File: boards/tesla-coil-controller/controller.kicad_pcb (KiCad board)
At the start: 2 copper layers, 163 x 141.8 mm, 331 parts, among them J1 DF40C-40DP-0.4V(51), J10 AUX 4 / 0-5V, J2 DF40C(2.0)-40DS-0.4V(51), J3 AUX 1 / 0-5V, J30 12V BATTERY / LOWER, J4 12V BATTERY / UPPER, J40 CST SECONDARY, J5 USB-C / PROGRAMMING ONLY, J50 GDT 1 PRIMARY, J51 GDT 2 PRIMARY, J60 CST 2 SECONDARY, J8 AUX 2 / 0-5V, J9 AUX 3 / 0-5V, Q50 STD80N10F7, Q51 STD80N10F7, Q52 STD80N10F7, Q53 STD80N10F7, Q54 STD80N10F7, Q55 STD80N10F7, Q56 STD80N10F7, Q57 STD80N10F7, U1 AD7606C-16BSTZ, U2 AP2112K-3.3, U3 USBLC6-2SC6, U30 LMZ14202HTZX/NOPB, U31 LMZ14202HTZX/NOPB, U40 OPA197IDBVR, U41 OPA197IDBVR, U42 TLV3501AIDBVR, U44 TPS60403DBVR, U51 UCC27282DR, U52 UCC27282DR, U53 UCC27282DR, U54 UCC27282DR, U60 OPA197IDBVR, U61 OPA197IDBVR, U62 TLV3501AIDBVR, U70 OPA197IDBVR, U71 OPA197IDBVR, U72 OPA197IDBVR, U73 OPA197IDBVR

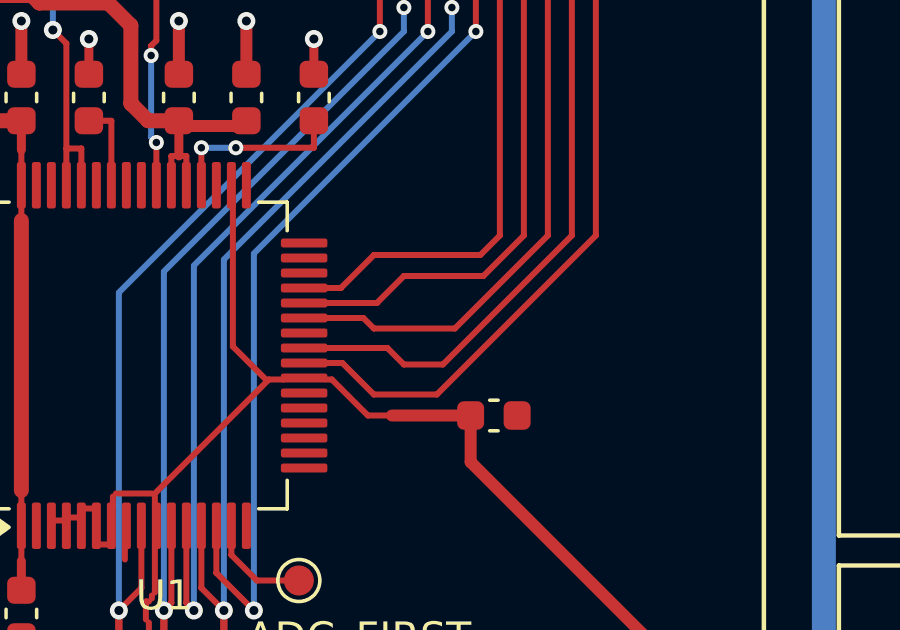
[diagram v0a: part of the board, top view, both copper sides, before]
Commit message: Groom the ADC data-line exits into one horizontal and one 45° climb each
Portal edit-stack item: "The lines to the right of the adc could be nicer
groomed". ADC_SDI and ADC_DOUT_A..D each left the ADC with a horizontal, a
45° jog to a different row (some up, some down, all different sizes), a
second horizontal, and a 45° climb into the 0.8 mm column bus at y=92. The
jogs did the 0.5 -> 0.8 mm pitch change and looked ragged.

Each line is now a single straight horizontal from its pad at its own pin
row, then one 45° climb landing on the same column endpoint as before. The
pitch change happens in the diagonal start points instead of mid-run jogs.
Four segments per net became two; the column verticals are untouched.

Generator-owned: tesla_reviewed_routing.json edited and replayed. No
footprints moved; only the five ADC nets changed. DRC 0/0/0. kct lint:
0 open; five flagged findings on these lines (four route.bend_count and the
ADC_DOUT_D route.redundant_bend) are resolved and their exceptions removed.
Evidence refreshed for the remaining 188 exceptions (132 ignored, 56 flagged).

Co-Authored-By: Claude Fable 5.1 <noreply@anthropic.com>
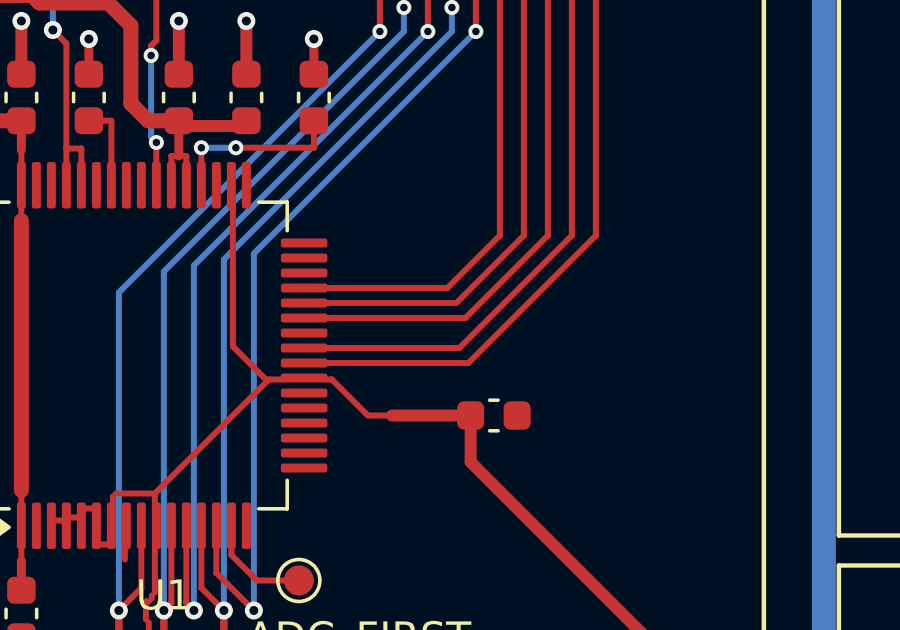
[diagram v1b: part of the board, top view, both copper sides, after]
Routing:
- net ADC_DOUT_A: track 36.2 -> 35.3 mm
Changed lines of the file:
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@@
 	(segment
 		(start 98.675 93.75)
-		(end 99.9 93.75)
-		(width 0.2)
-		(layer "F.Cu")
-		(net "ADC_SDI")
-	)
-	(segment
-		(start 104.55 92.65)
-		(end 101 92.65)
-		(width 0.2)
-		(layer "F.Cu")
-		(net "ADC_SDI")
-	)
-	(segment
-		(start 99.9 93.75)
-		(end 101 92.65)
-		(width 0.2)
-		(layer "F.Cu")
-		(net "ADC_SDI")
-	)
-	(segment
-		(start 105.2 92)
-		(end 104.55 92.65)
+		(end 103.45 93.75)
 		(width 0.2)
 		(layer "F.Cu")
@@
 	(segment
 		(start 105.2 68.82)
+		(end 105.2 92)
+		(width 0.2)
+		(layer "F.Cu")
+		(net "ADC_SDI")
+	)
+	(segment
+		(start 103.45 93.75)
 		(end 105.2 92)
 		(width 0.2)
@@
 	)
 	(segment
-		(start 98.675 94.25)
-		(end 101.1 94.25)
-		(width 0.2)
-		(layer "F.Cu")
-		(net "ADC_DOUT_D")
-	)
-	(segment
 		(start 105.6 71.6)
 		(end 106 72)
@@
 	)
 	(segment
-		(start 106 92)
-		(end 104.65 93.35)
+		(start 98.675 94.25)
+		(end 103.75 94.25)
 		(width 0.2)
 		(layer "F.Cu")
@@
 	)
 	(segment
-		(start 101.1 94.25)
-		(end 102 93.35)
+		(start 103.75 94.25)
+		(end 106 92)
 		(width 0.2)
 		(layer "F.Cu")
@@
 	)
 	(segment
-		(start 104.65 93.35)
-		(end 102 93.35)
-		(width 0.2)
-		(layer "F.Cu")
-		(net "ADC_DOUT_D")
-	)
-	(segment
-		(start 106.8 92)
-		(end 103.7 95.1)
-		(width 0.2)
-		(layer "F.Cu")
-		(net "ADC_DOUT_C")
-	)
-	(segment
-		(start 100.65 94.75)
-		(end 101 95.1)
-		(width 0.2)
-		(layer "F.Cu")
-		(net "ADC_DOUT_C")
-	)
-	(segment
-		(start 98.675 94.75)
-		(end 100.65 94.75)
-		(width 0.2)
-		(layer "F.Cu")
-		(net "ADC_DOUT_C")
-	)
-	(segment
 		(start 106 68.82)
 		(end 106 71.2)
-		(width 0.2)
-		(layer "F.Cu")
-		(net "ADC_DOUT_C")
-	)
-	(segment
-		(start 103.7 95.1)
-		(end 101 95.1)
 		(width 0.2)
 		(layer "F.Cu")
@@
 	)
 	(segment
+		(start 98.675 94.75)
+		(end 104.05 94.75)
+		(width 0.2)
+		(layer "F.Cu")
+		(net "ADC_DOUT_C")
+	)
+	(segment
 		(start 106.8 72)
+		(end 106.8 92)
+		(width 0.2)
+		(layer "F.Cu")
+		(net "ADC_DOUT_C")
+	)
+	(segment
+		(start 104.05 94.75)
 		(end 106.8 92)
 		(width 0.2)
@@
 	)
 	(segment
-		(start 103.3 96.3)
-		(end 102 96.3)
+		(start 98.675 95.75)
+		(end 103.85 95.75)
+		(width 0.2)
+		(layer "F.Cu")
+		(net "ADC_DOUT_B")
+	)
+	(segment
+		(start 103.85 95.75)
+		(end 107.6 92)
 		(width 0.2)
 		(layer "F.Cu")
@@
 	)
 	(segment
-		(start 107.6 92)
-		(end 103.3 96.3)
-		(width 0.2)
-		(layer "F.Cu")
-		(net "ADC_DOUT_B")
-	)
-	(segment
 		(start 106.4 70.8)
 		(end 107.6 72)
-		(width 0.2)
-		(layer "F.Cu")
-		(net "ADC_DOUT_B")
-	)
-	(segment
-		(start 101.45 95.75)
-		(end 102 96.3)
-		(width 0.2)
-		(layer "F.Cu")
-		(net "ADC_DOUT_B")
-	)
-	(segment
-		(start 98.675 95.75)
-		(end 101.45 95.75)
 		(width 0.2)
 		(layer "F.Cu")
@@
 	)
 	(segment
-		(start 108.4 91.999999)
-		(end 103.1 97.3)
-		(width 0.2)
-		(layer "F.Cu")
-		(net "ADC_DOUT_A")
-	)
-	(segment
-		(start 98.675 96.25)
-		(end 99.95 96.25)
-		(width 0.2)
-		(layer "F.Cu")
-		(net "ADC_DOUT_A")
-	)
-	(segment
 		(start 106.8 70.4)
 		(end 108.4 72)
@@
 	)
 	(segment
-		(start 99.95 96.25)
-		(end 101 97.3)
+		(start 104.15 96.25)
+		(end 108.4 92)
 		(width 0.2)
 		(layer "F.Cu")
@@
 	)
 	(segment
-		(start 103.1 97.3)
-		(end 101 97.3)
+		(start 98.675 96.25)
+		(end 104.15 96.25)
 		(width 0.2)
 		(layer "F.Cu")

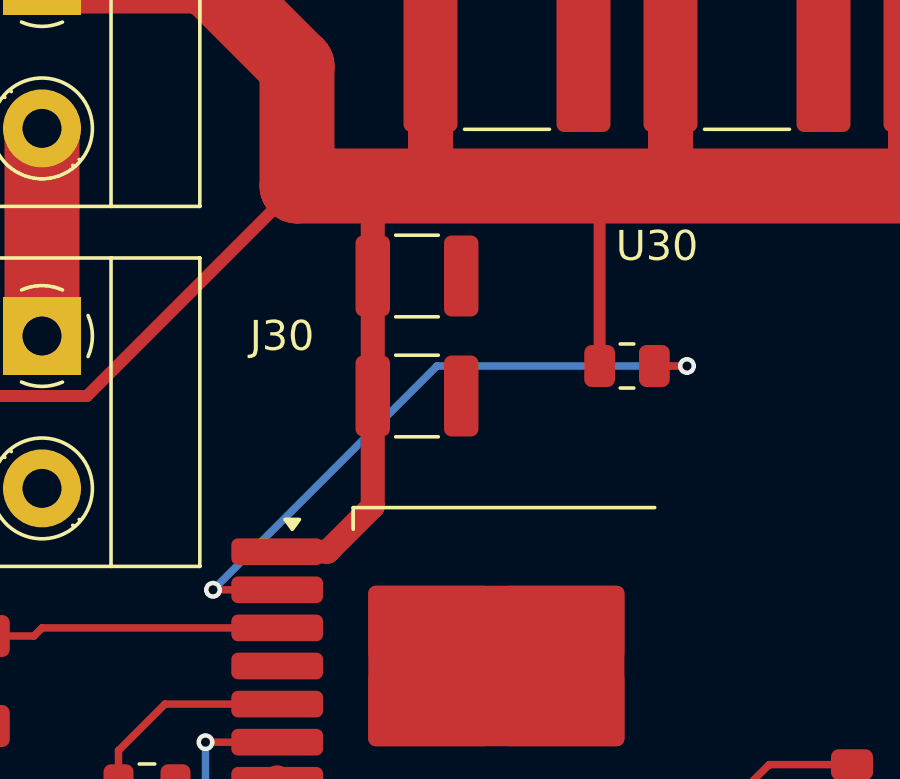
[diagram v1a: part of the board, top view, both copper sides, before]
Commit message: Move R302 next to U30 so P30_RON no longer runs under C302
Portal edit-stack item: "Move this guy so under-trace is unneeded". R302
(249k RON resistor) sat at (47,52) on the far side of the input caps, so
P30_RON dropped to B.Cu at its pad, ran 8 mm under C302, and came back up
beside U30 pin 2. R302 now sits at (35.1,55.55), rotated 180, in the gap
between J30's courtyard and the top of U30. RON leaves pad 2 straight,
wraps around U30 pin 1 at x=33.3 and enters pin 2 straight; VBAT leaves
pad 1 straight and tees into the 0.8 mm VBAT bus at full width. Both vias
and both B.Cu segments are gone, as is the old VBAT stub that fed R302
from the y=46 bus.

Also fixes the UUID suffixes of the ADC exit segments added in 5742a12
(non-hex characters made KiCad regenerate them on every replay).

Generator-owned: tesla_placement.json and tesla_reviewed_routing.json
edited and replayed. Only R302 moved; only P30_RON and VBAT_24V copper
changed. DRC 0/0/0 (kicad-cli and kicadmium). kct lint: 0 open, no new
findings; evidence refreshed for all 188 exceptions (132 ignored, 56 flagged).

Co-Authored-By: Claude Fable 5.1 <noreply@anthropic.com>
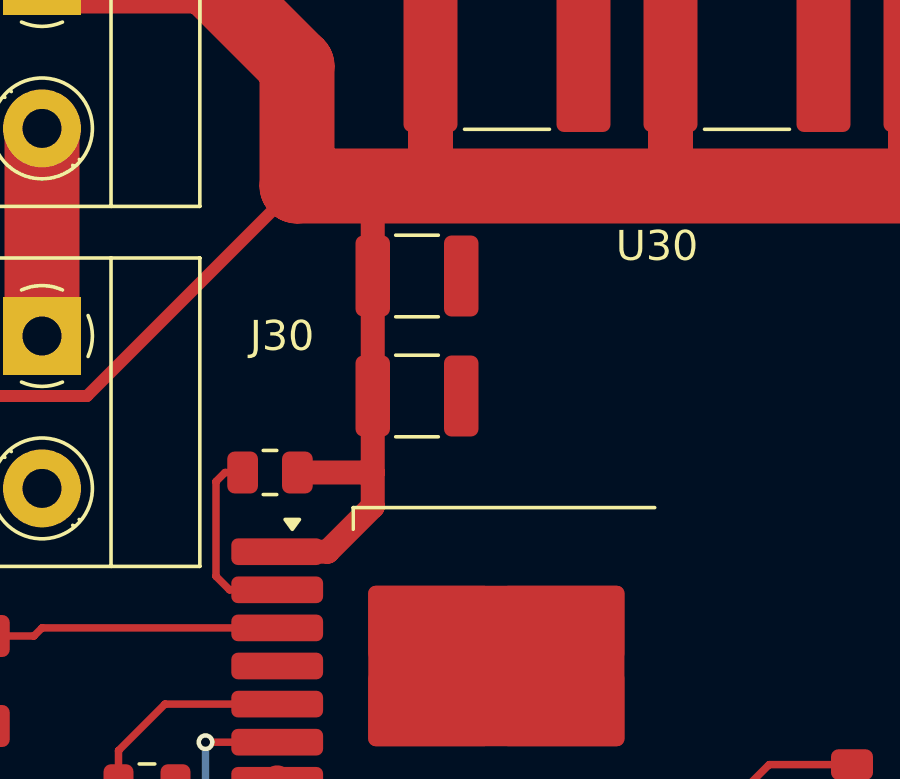
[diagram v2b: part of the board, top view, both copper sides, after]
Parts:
- moved R302 12.4 mm to (35.1, 55.5), turned to 180 degrees
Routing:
- net P30_RON: track 22.1 -> 6.40 mm, vias 2 -> 0
- net VBAT_24V: track 607.8 -> 604.3 mm
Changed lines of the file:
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@@
 	(footprint "Tesla:R_0805_2012Metric"
 		(layer "F.Cu")
-		(at 47 52)
+		(at 35.1 55.55 180)
 		(descr "Resistor SMD 0805 (2012 Metric), square (rectangular) end terminal, IPC_7351 nominal, (Body size source: IPC-SM-782 page 72, https://www.pcb-3d.com/wordpress/wp-content/uploads/ipc-sm-782a_amendment_1_and_2.pdf), generated with kicad-footprint-generator")
 		(tags "resistor")
 		(property "Reference" "R302"
-			(at 0 -5 0)
+			(at 0 1.1 180)
 			(layer "F.SilkS")
 			(hide yes)
@@
 		)
 		(property "Value" "249k"
-			(at 0 1.65 0)
+			(at 0 1.65 180)
 			(layer "F.Fab")
 			(hide yes)
@@
 		)
 		(property "Datasheet" ""
-			(at 0 0 0)
+			(at 0 0 180)
 			(layer "F.Fab")
 			(hide yes)
@@
 		)
 		(property "Description" ""
-			(at 0 0 0)
+			(at 0 0 180)
 			(layer "F.Fab")
 			(hide yes)
@@
 		)
 		(property "MPN" ""
-			(at 0 0 0)
+			(at 0 0 180)
 			(layer "F.SilkS")
 			(hide yes)
@@
 		)
 		(property "LCSC" ""
-			(at 0 0 0)
+			(at 0 0 180)
 			(layer "F.SilkS")
 			(hide yes)
@@
 		)
 		(property "Design status" "Acquisition draft / not for fabrication"
-			(at 0 0 0)
+			(at 0 0 180)
 			(layer "F.SilkS")
 			(hide yes)
@@
 		(duplicate_pad_numbers_are_jumpers no)
 		(fp_line
-			(start -0.227064 -0.735)
-			(end 0.227064 -0.735)
+			(start -0.227064 0.735)
+			(end 0.227064 0.735)
 			(stroke
 				(width 0.12)
@@
 		)
 		(fp_line
-			(start -0.227064 0.735)
-			(end 0.227064 0.735)
+			(start -0.227064 -0.735)
+			(end 0.227064 -0.735)
 			(stroke
 				(width 0.12)
@@
 		)
 		(fp_line
-			(start -1.68 -0.95)
-			(end 1.68 -0.95)
+			(start 1.68 0.95)
+			(end -1.68 0.95)
 			(stroke
 				(width 0.05)
@@
 		)
 		(fp_line
-			(start -1.68 0.95)
-			(end -1.68 -0.95)
+			(start 1.68 -0.95)
+			(end 1.68 0.95)
 			(stroke
 				(width 0.05)
@@
 		)
 		(fp_line
-			(start 1.68 -0.95)
-			(end 1.68 0.95)
+			(start -1.68 0.95)
+			(end -1.68 -0.95)
 			(stroke
 				(width 0.05)
@@
 		)
 		(fp_line
-			(start 1.68 0.95)
-			(end -1.68 0.95)
+			(start -1.68 -0.95)
+			(end 1.68 -0.95)
 			(stroke
 				(width 0.05)
@@
 		)
 		(fp_line
-			(start -1 -0.625)
-			(end 1 -0.625)
+			(start 1 0.625)
+			(end -1 0.625)
 			(stroke
 				(width 0.1)
@@
 		)
 		(fp_line
-			(start -1 0.625)
-			(end -1 -0.625)
+			(start 1 -0.625)
+			(end 1 0.625)
 			(stroke
 				(width 0.1)
@@
 		)
 		(fp_line
-			(start 1 -0.625)
-			(end 1 0.625)
+			(start -1 0.625)
+			(end -1 -0.625)
 			(stroke
 				(width 0.1)
@@
 		)
 		(fp_line
-			(start 1 0.625)
-			(end -1 0.625)
+			(start -1 -0.625)
+			(end 1 -0.625)
 			(stroke
 				(width 0.1)
@@
 		)
 		(fp_text user "${REFERENCE}"
-			(at 0 0 0)
+			(at 0 0 180)
 			(layer "F.Fab")
 			(effects
@@
 		)
 		(pad "1" smd roundrect
-			(at -0.9125 0)
+			(at -0.9125 0 180)
 			(size 1.025 1.4)
 			(layers "F.Cu" "F.Mask" "F.Paste")
@@
 		)
 		(pad "2" smd roundrect
-			(at 0.9125 0)
+			(at 0.9125 0 180)
 			(size 1.025 1.4)
 			(layers "F.Cu" "F.Mask" "F.Paste")
@@
 	)
 	(segment
+		(start 36.0125 55.55)
+		(end 38.525 55.55)
+		(width 0.8)
+		(layer "F.Cu")
+		(net "VBAT_24V")
+	)
+	(segment
 		(start 71.525 56.685)
 		(end 70.02 58.19)
@@
 	)
 	(segment
-		(start 46.0875 46)
-		(end 46.0875 52)
-		(width 0.4)
-		(layer "F.Cu")
-		(net "VBAT_24V")
-	)
-	(segment
 		(start 35 39)
 		(end 34 40)
@@
 	)
 	(segment
-		(start 105.2 68.82)
+		(start 103.45 93.75)
 		(end 105.2 92)
 		(width 0.2)
@@
 	)
 	(segment
-		(start 103.45 93.75)
+		(start 105.2 68.82)
 		(end 105.2 92)
 		(width 0.2)
@@
 	)
 	(segment
-		(start 105.6 71.6)
-		(end 106 72)
+		(start 98.675 94.25)
+		(end 103.75 94.25)
 		(width 0.2)
 		(layer "F.Cu")
@@
 	)
 	(segment
-		(start 98.675 94.25)
-		(end 103.75 94.25)
+		(start 103.75 94.25)
+		(end 106 92)
 		(width 0.2)
 		(layer "F.Cu")
@@
 	)
 	(segment
-		(start 103.75 94.25)
-		(end 106 92)
+		(start 105.6 71.6)
+		(end 106 72)
 		(width 0.2)
 		(layer "F.Cu")
@@
 	)
 	(segment
-		(start 106 68.82)
-		(end 106 71.2)
+		(start 98.675 94.75)
+		(end 104.05 94.75)
 		(width 0.2)
 		(layer "F.Cu")
@@
 	)
 	(segment
-		(start 106 71.2)
-		(end 106.8 72)
+		(start 104.05 94.75)
+		(end 106.8 92)
 		(width 0.2)
 		(layer "F.Cu")
@@
 	)
 	(segment
-		(start 98.675 94.75)
-		(end 104.05 94.75)
+		(start 106 68.82)
+		(end 106 71.2)
 		(width 0.2)
 		(layer "F.Cu")
@@
 	)
 	(segment
-		(start 106.8 72)
-		(end 106.8 92)
+		(start 106 71.2)
+		(end 106.8 72)
 		(width 0.2)
 		(layer "F.Cu")
@@
 	)
 	(segment
-		(start 104.05 94.75)
+		(start 106.8 72)
 		(end 106.8 92)
 		(width 0.2)
@@
 	)
 	(segment
-		(start 106.8 70.4)
-		(end 108.4 72)
+		(start 98.675 96.25)
+		(end 104.15 96.25)
 		(width 0.2)
 		(layer "F.Cu")
@@
 	)
 	(segment
-		(start 98.675 96.25)
-		(end 104.15 96.25)
+		(start 106.8 70.4)
+		(end 108.4 72)
 		(width 0.2)
 		(layer "F.Cu")
@@
 	)
 	(segment
-		(start 47.9125 52)
-		(end 49 52)
+		(start 34.1875 55.55)
+		(end 33.6 55.55)
 		(width 0.25)
 		(layer "F.Cu")
@@
 	)
 	(segment
-		(start 35.34 59.46)
-		(end 33.2 59.46)
+		(start 33.6 55.55)
+		(end 33.3 55.85)
 		(width 0.25)
 		(layer "F.Cu")
 		(net "P30_RON")
 	)
-	(via
-		(at 33.2 59.46)
-		(size 0.6)
-		(drill 0.3)
-		(layers "F.Cu" "B.Cu")
-		(net "P30_RON")
-	)
-	(via
-		(at 49 52)
-		(size 0.6)
-		(drill 0.3)
-		(layers "F.Cu" "B.Cu")
+	(segment
+		(start 33.3 55.85)
+		(end 33.3 59.01)
+		(width 0.25)
+		(layer "F.Cu")
 		(net "P30_RON")
 	)
 	(segment
-		(start 40.66 52)
-		(end 33.2 59.46)
+		(start 33.3 59.01)
+		(end 33.75 59.46)
 		(width 0.25)
-		(layer "B.Cu")
+		(layer "F.Cu")
 		(net "P30_RON")
 	)
 	(segment
-		(start 49 52)
-		(end 40.66 52)
+		(start 33.75 59.46)
+		(end 35.34 59.46)
 		(width 0.25)
-		(layer "B.Cu")
+		(layer "F.Cu")
 		(net "P30_RON")
 	)
